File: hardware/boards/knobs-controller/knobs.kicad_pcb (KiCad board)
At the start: 2 copper layers, 110.5 x 111.1 mm, 175 parts, among them J1 ZX62-AB-5PA(31), J10 Conn_01x01_Female, J11 Conn_01x01_Female, J12 Conn_01x01_Female, J13 Conn_01x01_Female, J14 Conn_01x01_Female, J15 Conn_01x01_Female, J16 Conn_01x01_Female, J17 Conn_01x01_Female, J18 Conn_01x01_Female, J19 Conn_01x01_Female, J2 2X3_SMD_MALE, J20 Conn_01x01_Female, J21 Conn_01x01_Female, J22 Conn_01x01_Female, J23 Conn_01x01_Female, J24 Conn_01x01_Female, J25 Conn_01x01_Female, J26 Conn_01x01_Female, J27 Conn_01x01_Female, J28 Conn_01x01_Female, J29 Conn_01x01_Female, J3 Conn_01x01_Female, J30 Conn_01x01_Female, J31 Conn_01x01_Female, J32 Conn_01x01_Female, J33 Conn_01x01_Female, J34 Conn_01x01_Female, J35 Conn_01x01_Female, J36 Conn_01x01_Female, J37 Conn_01x01_Female, J38 Conn_01x01_Female, J39 Conn_01x01_Female, J4 Conn_01x01_Female, J40 Conn_01x01_Female, J41 Conn_01x01_Female, J42 Conn_01x01_Female, J43 Conn_01x01_Female, J44 Conn_01x01_Female, J45 Conn_01x01_Female, J46 Conn_01x01_Female, J47 Conn_01x01_Female, J48 Conn_01x01_Female, J49 Conn_01x01_Female, J5 Conn_01x01_Female, J50 Conn_01x01_Female, J51 Conn_01x01_Female, J52 Conn_01x01_Female, J53 Conn_01x01_Female, J54 Conn_01x01_Female, J55 Conn_01x01_Female, J56 Conn_01x01_Female, J57 WURTH_ELECTRONICS_61400413321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, J58 USB-A-S-X-X-VT, J59 ST7735_1.4, J6 Conn_01x01_Female, J7 Conn_01x01_Female, J8 Conn_01x01_Female, J9 Conn_01x01_Female, SW1 Rotary Encoder, SW2 Rotary Encoder, SW3 Rotary Encoder, U1 ATSAMD21G18A-48, U2 AP7215-33YG-13, U3 ANALOG_DEVICES_AD7606BSTZANAL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, U4 ANALOG_DEVICES_AD5754BREZANAL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, U5 MICROCHIP_MCP1700T-2502E-TTMI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, Y1 32.768KHz

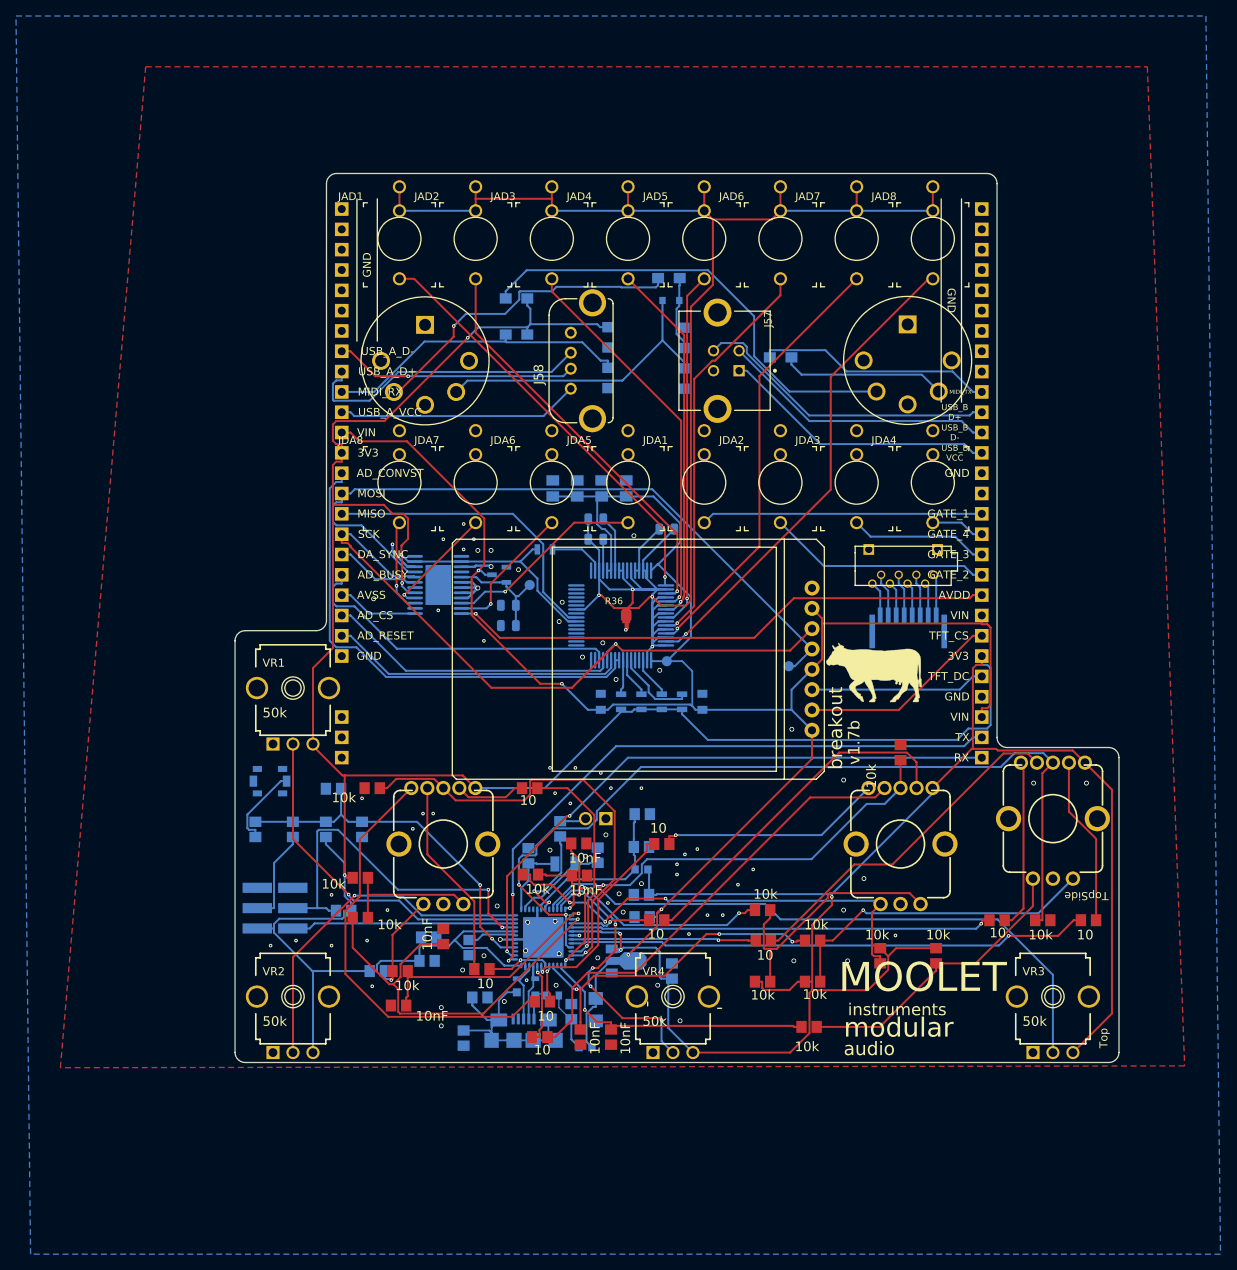
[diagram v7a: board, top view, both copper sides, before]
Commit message: refactor footprints schematics
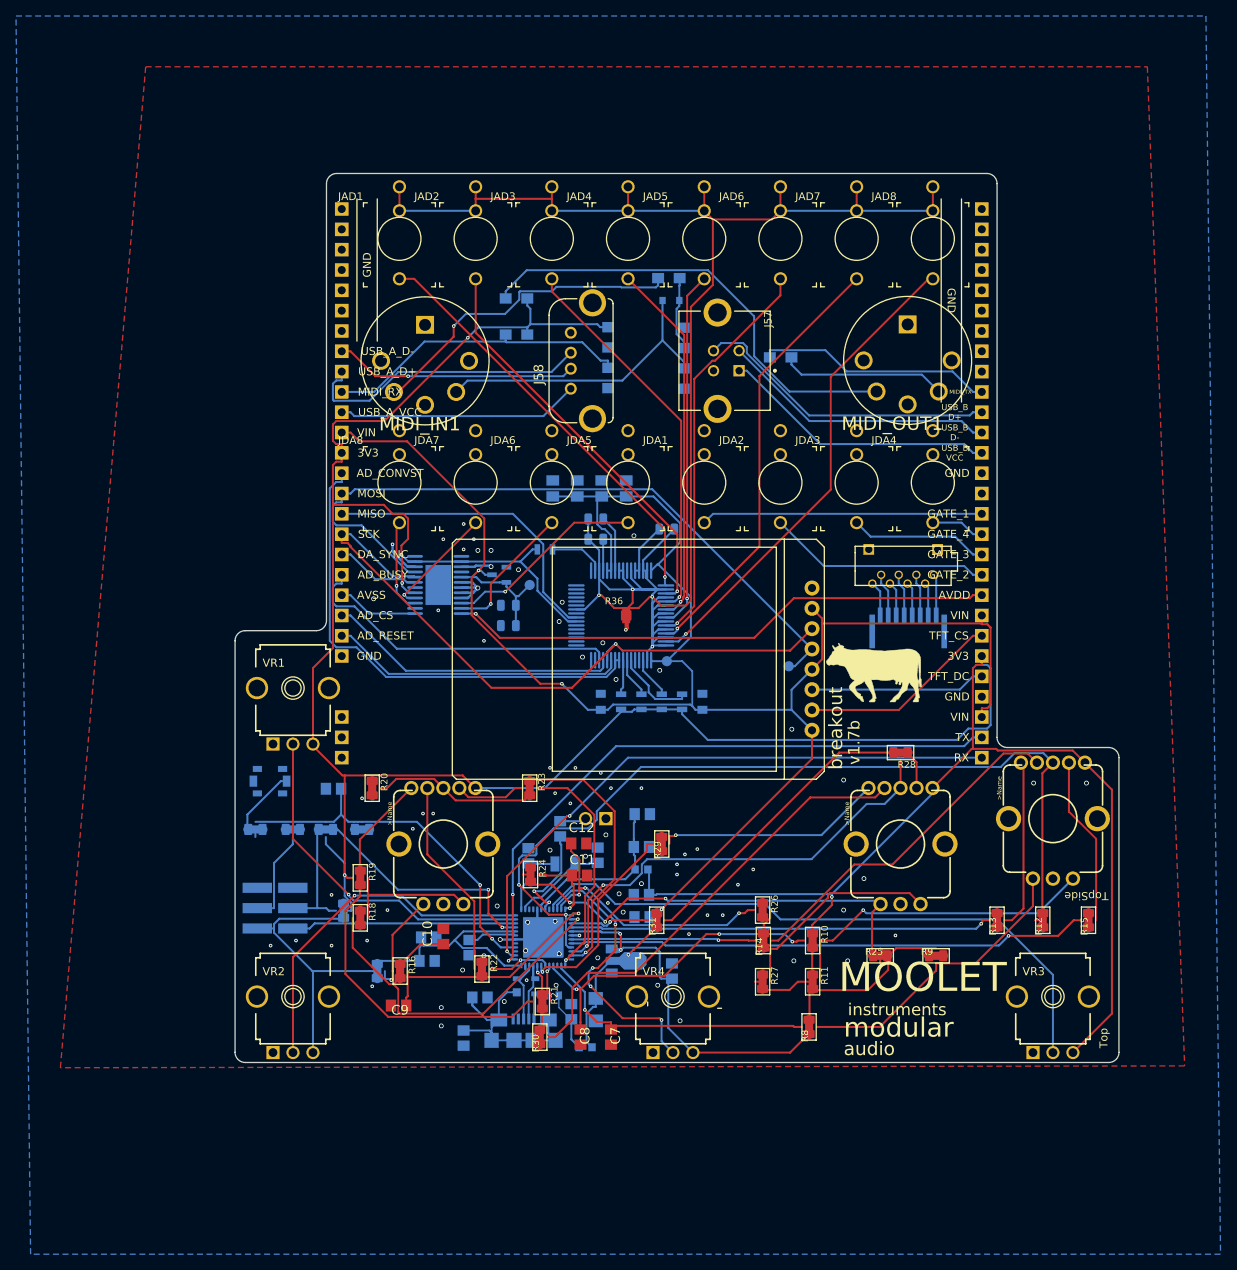
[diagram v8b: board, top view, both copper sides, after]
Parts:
- C1, C13, C14, C15, C16, C17, C18, C19, C2, C20, C4, C5: footprint knobs:RESISTOR-NICK_C0805 -> footprints:RESISTOR-NICK_C0805
- C10, C11, C12, C3, C7, C8, C9: footprint knobs:C0805 -> footprints:C0805
- C21, C22, C23, C24: footprint topbreakout:C0805K -> footprints:C0805K
- C6: footprint knobs:RESISTOR-NICK_C1206 -> footprints:RESISTOR-NICK_C1206
- D1: footprint knobs:MK1_ZERO_SOT190P230X110-4N -> footprints:MK1_ZERO_SOT190P230X110-4N
- D2: footprint knobs:LED_RADIAL_3MM -> footprints:LED_RADIAL_3MM
- F1: footprint knobs:MK1_ZERO_0603-F1608X100N -> footprints:MK1_ZERO_0603-F1608X100N
- J1: footprint knobs:MK1_ZERO_USBMICRO-ZX62-AB-5PA -> footprints:MK1_ZERO_USBMICRO-ZX62-AB-5PA
- J2: footprint knobs:2X3_SMT -> footprints:2X3_SMT
- J57: footprint topbreakout:WURTH_ELECTRONICS_61400413321_0 -> footprints:WURTH_ELECTRONICS_61400413321_0
- J58: footprint topbreakout:USB-A-S-X-X-VT -> footprints:USB-A-S-X-X-VT
- J59: footprint topbreakout:ST7735 -> footprints:ST7735
- JAD1, JAD2, JAD3, JAD4, JAD5, JAD6, JAD7, JAD8, JDA1, JDA2, JDA3, JDA4, JDA5, JDA6, JDA7, JDA8: footprint topbreakout:WQP-PJ301M-12_JACK -> footprints:WQP-PJ301M-12_JACK
- L1, L2: footprint knobs:MK1_ZERO_0603-1608X90N -> footprints:MK1_ZERO_0603-1608X90N
- MIDI_IN1, MIDI_OUT1: footprint topbreakout:OG-MIDI_SD-50BV -> footprints:OG-MIDI_SD-50BV
- R1, R7: footprint knobs:RESISTOR-NICK_R0805 -> footprints:RESISTOR-NICK_R0805
- R10, R11, R12, R13, R14, R15, R16, R17, R18, R19, R2, R20, R21, R22, R23, R24, R25, R26, R27, R28, R29, R3, R30, R31, R4, R5, R6, R8, R9: footprint knobs:R0805 -> footprints:R0805
- R36: footprint Mainboard:NetTie-I_Connected_SMD_small -> footprints:NetTie-I_Connected_SMD_small
- SW1, SW2, SW3: footprint knobs:ENCODER_LED_3_KIT -> footprints:ENCODER_LED_3_KIT
- TP1, TP2, TP3: footprint topbreakout:PAD.03X.05 -> footprints:PAD.03X.05
- U$1: footprint knobs:C&K_PTS820_NOPEGS -> footprints:C&K_PTS820_NOPEGS
- U$2: footprint topbreakout:YAMAICHI_MICROSD_VERTICAL -> footprints:YAMAICHI_MICROSD_VERTICAL
- U$3: footprint common:HFW8R-1STE1LF -> footprints:HFW8R-1STE1LF
- U$4: footprint Mainboard:8-SMD -> footprints:8-SMD
- U1: footprint knobs:MK1_ZERO_QFN50P700X700X90-49XN-EPSQ515 -> footprints:MK1_ZERO_QFN50P700X700X90-49XN-EPSQ515
- U2: footprint knobs:MK1_ZERO_SOT150P400X160-3N -> footprints:MK1_ZERO_SOT150P400X160-3N
- U3: footprint topbreakout:ANALOG_DEVICES_AD7606BSTZ_2 -> footprints:ANALOG_DEVICES_AD7606BSTZ_2
- U4: footprint topbreakout:ANALOG_DEVICES_AD5754BREZ_2 -> footprints:ANALOG_DEVICES_AD5754BREZ_2
- U5: footprint topbreakout:MICROCHIP_MCP1700T-2502E-TT_0 -> footprints:MICROCHIP_MCP1700T-2502E-TT_0
- VR1, VR2, VR3, VR4: footprint knobs:MUSICTHINGMODULAR_9MM_SNAP-IN_POT -> footprints:MUSICTHINGMODULAR_9MM_SNAP-IN_POT
- Y1: footprint knobs:MK1_ZERO_QUARZO-ABS07 -> footprints:MK1_ZERO_QUARZO-ABS07
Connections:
- J1 pad 4: (no net) -> Net-(J1-Pad4)
- J2 pad 6: (no net) -> Net-(J2-Pad6)
- J57 pad 5: (no net) -> Net-(J57-Pad5)
- J57 pad 6: (no net) -> Net-(J57-Pad6)
- J58 pad G1: (no net) -> Net-(J58-PadG1)
- J58 pad G2: (no net) -> Net-(J58-PadG2)
- JDA1 pad P$2_SWITCH: (no net) -> Net-(JDA1-PadP$2_SWITCH)
- JDA2 pad P$2_SWITCH: (no net) -> Net-(JDA2-PadP$2_SWITCH)
- JDA3 pad P$2_SWITCH: (no net) -> Net-(JDA3-PadP$2_SWITCH)
- JDA4 pad P$2_SWITCH: (no net) -> Net-(JDA4-PadP$2_SWITCH)
- JDA5 pad P$2_SWITCH: (no net) -> Net-(JDA5-PadP$2_SWITCH)
- JDA6 pad P$2_SWITCH: (no net) -> Net-(JDA6-PadP$2_SWITCH)
- JDA7 pad P$2_SWITCH: (no net) -> Net-(JDA7-PadP$2_SWITCH)
- JDA8 pad P$2_SWITCH: (no net) -> Net-(JDA8-PadP$2_SWITCH)
- MIDI_IN1 pad 1: (no net) -> Net-(MIDI_IN1-Pad1)
- MIDI_IN1 pad 2: (no net) -> Net-(MIDI_IN1-Pad2)
- MIDI_IN1 pad 3: (no net) -> Net-(MIDI_IN1-Pad3)
- MIDI_OUT1 pad 1: (no net) -> Net-(MIDI_OUT1-Pad1)
- MIDI_OUT1 pad 2: (no net) -> Net-(MIDI_OUT1-Pad2)
- MIDI_OUT1 pad 3: (no net) -> Net-(MIDI_OUT1-Pad3)
- R6 pad 2: (no net) -> /knobs_1/RESET#
- U$2 pad GND1: (no net) -> Net-(U$2-PadGND1)
- U$2 pad GND2: (no net) -> Net-(U$2-PadGND2)
- U$3 pad 10: (no net) -> Net-(U$3-Pad10)
- U$3 pad 9: (no net) -> Net-(U$3-Pad9)
- U1 pad 24: (no net) -> /knobs_1/PA15_S2_MISO
- U1 pad 27: (no net) -> Net-(U1-Pad27)
- U1 pad 3: (no net) -> /knobs_1/PA02_AIN0
- U1 pad 39: (no net) -> /knobs_1/PA27_CD
- U1 pad 4: (no net) -> /knobs_1/PA03_VREFA
- U1 pad 41: (no net) -> Net-(U1-Pad41)
- U1 pad 8: (no net) -> /knobs_1/PB09_ADC
- U3 pad 15: (no net) -> Net-(U3-Pad15)
- U3 pad 42: (no net) -> /AD7606/AD_REFINOUT
- U4 pad 12: (no net) -> Net-(U4-Pad12)
- U4 pad 13: (no net) -> Net-(U4-Pad13)
- U4 pad 16: (no net) -> Net-(U4-Pad16)
- U4 pad 2: (no net) -> Net-(U4-Pad2)
- U4 pad 25: (no net) -> Net-(U4-Pad25)
- U4 pad 6: (no net) -> Net-(U4-Pad6)
